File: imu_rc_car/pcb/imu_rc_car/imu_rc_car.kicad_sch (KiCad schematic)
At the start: 27 parts, among them J1 Encoder FS, J10 Prox Sensor RS, J11 Prox Sensor LS, J12 Prox Sensor BS, J2 Encoder BS, J7 Left Terminal, J8 Right Terminal, J9 Prox Sensor FS, Q5 IRLML6344TRPBF, Q6 DMP3160L-7, U1 ESP32-S3-DevKitC, U2 TB6612FNG, U3 AP2112K-3.3, U4 TB6612FNG

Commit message: commit #27
revision for hand unit complete (board is ready)
board for proximity sensors in series
minor revision in encoder board
progressing work in car board
added essential libraries support for 3D components
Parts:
- removed C7, C8: 1uF/16V, Capacitor_SMD:C_0805_2012Metric, symbol Device:C_Small
- removed J10: Prox Sensor RS, Connector_JST:JST_PH_S5B-PH-K_1x05_P2.00mm_Horizontal, symbol Connector:Conn_01x05_Socket
- removed J11: Prox Sensor LS, Connector_JST:JST_PH_S5B-PH-K_1x05_P2.00mm_Horizontal, symbol Connector:Conn_01x05_Socket
- removed J12: Prox Sensor BS, Connector_JST:JST_PH_S5B-PH-K_1x05_P2.00mm_Horizontal, symbol Connector:Conn_01x05_Socket
- removed J2: Encoder BS, Connector_JST:JST_PH_S4B-PH-K_1x04_P2.00mm_Horizontal, symbol Connector:Conn_01x04_Socket
- removed U3: AP2112K-3.3, Package_TO_SOT_SMD:SOT-23-5, symbol Regulator_Linear:AP2112K-3.3
- added C1: 10uF, Capacitor_SMD:CP_Elec_5x5.7, symbol Device:C_Polarized
- added J1: LiPo Battery, IMURCLibrary:AMASS_XT60IPW-M_1x03_P7.20mm_Horizontal, symbol Connector:Conn_01x02_Socket
- added J3: Encoder B, IMURCLibrary:JST_PH_S4B-PH-SM4-TB_1x04-1MP_P2.00mm_Horizontal, symbol Connector:Conn_01x04_Socket
- added J5: Prox Sensor LS, IMURCLibrary:JST_PH_S5B-PH-SM4-TB_1x05-1MP_P2.00mm_Horizontal, symbol Connector:Conn_01x05_Socket
- added J6: Prox Sensor RS, IMURCLibrary:JST_PH_S5B-PH-SM4-TB_1x05-1MP_P2.00mm_Horizontal, symbol Connector:Conn_01x05_Socket
- added J7: Prox Sensor BS, IMURCLibrary:JST_PH_S5B-PH-SM4-TB_1x05-1MP_P2.00mm_Horizontal, symbol Connector:Conn_01x05_Socket
- added JP1: SolderJumper_2_Open, Jumper:SolderJumper-2_P1.3mm_Open_RoundedPad1.0x1.5mm, symbol Jumper:SolderJumper_2_Open
- added SW1: SW_Nidec_CAS-120A1, Button_Switch_SMD:Nidec_Copal_CAS-120A, symbol Switch:SW_Nidec_CAS-120A1
- J2: renamed from J1; value Encoder FS -> Encoder F; footprint Connector_JST:JST_PH_S4B-PH-K_1x04_P2.00mm_Horizontal -> IMURCLibrary:JST_PH_S4B-PH-SM4-TB_1x04-1MP_P2.00mm_Horizontal
- J4: renamed from J9; footprint Connector_JST:JST_PH_S5B-PH-K_1x05_P2.00mm_Horizontal -> IMURCLibrary:JST_PH_S5B-PH-SM4-TB_1x05-1MP_P2.00mm_Horizontal
- J8: renamed from J7; footprint TerminalBlock:TerminalBlock_Xinya_XY308-2.54-4P_1x04_P2.54mm_Horizontal -> IMURCLibrary:TerminalBlock_Xinya_XY308-2.54-4P_1x04_P2.54mm_Horizontal
- J9: renamed from J8; footprint TerminalBlock:TerminalBlock_Xinya_XY308-2.54-4P_1x04_P2.54mm_Horizontal -> IMURCLibrary:TerminalBlock_Xinya_XY308-2.54-4P_1x04_P2.54mm_Horizontal
- R10: value 6k -> 51k
- R9: value 22k -> 33k
- U1: footprint PCM_Espressif:ESP32-S3-DevKitC -> IMURCLibrary:ESP32-S3-DevKitC
- renumbered Q6 to Q1, Q5 to Q2, U4 to U3
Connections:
- net 7.4V is gone; now on net +7V4: C11.1, C12.1, C15.1, C16.1, U2.13 (VM2), U2.14 (VM3), U2.24 (VM1), U3.13 (VM2), U3.14 (VM3), U3.24 (VM1)
- net SI is gone; now on net +7V4: J4.4 (Pin_4)
- net +3V3: now also J3.4 (Pin_4), J5.3 (Pin_3), J6.3 (Pin_3), J7.3 (Pin_3)
- net ENC3: now also J3.2 (Pin_2)
- net ENC4: now also J3.1 (Pin_1)
- net GND: now also C1.2, J1.1 (Pin_1), J3.3 (Pin_3), J5.2 (Pin_2), J6.2 (Pin_2), J7.2 (Pin_2)
- net PRX_BS: now also J7.1 (Pin_1)
- net PRX_LS: now also J5.1 (Pin_1)
- net PRX_RS: now also J6.1 (Pin_1)
- net SO: now also J7.5 (Pin_5)
- net at J4.5 (Pin_5): now also J5.4 (Pin_4), JP1.2 (B)
- net +BATT renamed +7V4
- net +7V4: now also C1.1, SW1.1 (C)
- net MOTOR1+ renamed MOTOR_FL+
- net MOTOR_FL+: now also J8.1 (Pin_1); no longer J8.2 (Pin_2)
- net MOTOR1- renamed MOTOR_FL-
- net MOTOR_FL-: now also J8.2 (Pin_2); no longer J8.1 (Pin_1)
- net MOTOR2+ renamed MOTOR_RL+
- net MOTOR2- renamed MOTOR_RL-
- net MOTOR3+ renamed MOTOR_RR+
- net MOTOR_RR+: now also J9.1 (Pin_1); no longer J9.2 (Pin_2)
- net MOTOR3- renamed MOTOR_RR-
- net MOTOR_RR-: now also J9.2 (Pin_2); no longer J9.1 (Pin_1)
- net MOTOR4+ renamed MOTOR_FR+
- net MOTOR4- renamed MOTOR_FR-
- new net: J5.5 (Pin_5), J6.4 (Pin_4)
- new net: J1.2 (Pin_2), SW1.2 (B)
- new net: J6.5 (Pin_5), J7.4 (Pin_4), JP1.1 (A)
- no-connect marks 0 -> 1
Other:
- note added: "Battery"
- note removed: "Voltage Regulator"
- moved on the sheet: C10, C11, C12, C13, C14, C15, C16, C9, J2, J4, J8, J9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

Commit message: commit #28
added 3d file for esp32s3
progression with car pcb
minor changes prox sensors test board
final revision hand unit
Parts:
- removed C10, C12, C14, C16: 10uF, Capacitor_SMD:C_1206_3216Metric_Pad1.33x1.80mm_HandSolder, symbol Device:C
- removed C11, C13, C15, C9: 0.1uF, Capacitor_SMD:C_1206_3216Metric_Pad1.33x1.80mm_HandSolder, symbol Device:C
- removed U2, U3: TB6612FNG, Package_SO:SSOP-24_5.3x8.2mm_P0.65mm, symbol Driver_Motor:TB6612FNG
- added C10, C12: 2.2uF, Capacitor_SMD:C_0805_2012Metric, symbol Device:C_Small
- added C11, C9: 10nF, Capacitor_SMD:C_0805_2012Metric, symbol Device:C_Small
- added C13, C15: 100nF, Capacitor_SMD:C_0805_2012Metric, symbol Device:C_Small
- added C14, C8: 10uF, Capacitor_SMD:C_0805_2012Metric, symbol Device:C_Small
- added Q1: IRLZ34N, Package_TO_SOT_SMD:TO-263-2_TabPin1, symbol Transistor_FET:IRLZ34N
- added R11: 22, Resistor_SMD:R_0805_2012Metric, symbol Device:R_US
- added R12: 100k, Resistor_SMD:R_0805_2012Metric, symbol Device:R_US
- added U3: AMS1117-3.3, Package_TO_SOT_SMD:SOT-223-3_TabPin2, symbol Regulator_Linear:AMS1117-3.3
- added U6, U7: DRV8833PWP, Package_SO:HTSSOP-16-1EP_4.4x5mm_P0.65mm_EP3.4x5mm_Mask2.46x2.31mm_ThermalVias, symbol Driver_Motor:DRV8833PWP
- J3: renamed from J1; footprint IMURCLibrary:AMASS_XT60IPW-M_1x03_P7.20mm_Horizontal -> TerminalBlock:TerminalBlock_MaiXu_MX126-5.0-02P_1x02_P5.00mm
- SW1: footprint Button_Switch_SMD:Nidec_Copal_CAS-120A -> Button_Switch_THT:SW_Slide_SPDT_Angled_CK_OS102011MA1Q
- U1: footprint IMURCLibrary:ESP32-S3-DevKitC -> PCM_Espressif:ESP32-S3-DevKitC
- renumbered J2 to J1, J5 to J10, J6 to J11, J7 to J12, J3 to J2, J8 to J7, J9 to J8, J4 to J9, Q2 to Q5, Q1 to Q6
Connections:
- net PWMA is gone; now on net BIN3: U1.6 (GPIO6/ADC1_CH5)
- net PWMB is gone; now on net BIN4: U1.7 (GPIO7/ADC1_CH6)
- net +3V3: now also C15.1, C8.1, U3.2 (VO)
- net +7V4: now also C10.1, C12.1, C13.1, C14.1, Q1.1 (G), R12.1, U3.3 (VI), U6.12 (VM), U6.14 (VINT), U7.12 (VM), U7.14 (VINT)
- net AIN1: now also U1.32 (GPIO35), U7.16 (AIN1); no longer U1.4 (GPIO4/ADC1_CH3)
- net AIN2: now also U1.30 (GPIO45), U7.15 (AIN2); no longer U1.5 (GPIO5/ADC1_CH4)
- net AIN3: now also U1.9 (GPIO16/ADC2_CH5/32K_N), U6.16 (AIN1); no longer U1.17 (GPIO11/ADC2_CH0)
- net AIN4: now also U1.8 (GPIO15/ADC2_CH4/32K_P), U6.15 (AIN2); no longer U1.18 (GPIO12/ADC2_CH1)
- net BATT_READ: now also U1.26 (GPIO20/USB_D+); no longer U1.32 (GPIO35)
- net BATT_READ_EN: now also U1.27 (GPIO21); no longer U1.33 (GPIO36)
- net BIN1: now also U1.28 (GPIO47), U7.9 (BIN1); no longer U1.11 (GPIO18/ADC2_CH7)
- net BIN2: now also U1.29 (GPIO48), U7.10 (BIN2); no longer U1.25 (GPIO19/USB_D-)
- net BIN3: now also U6.9 (BIN1); no longer U1.26 (GPIO20/USB_D+)
- net BIN4: now also U6.10 (BIN2); no longer U1.27 (GPIO21)
- net ENC1: now also U1.38 (GPIO41/MTDI)
- net ENC2: now also U1.39 (GPIO42/MTMS)
- net ENC3: now also U1.37 (GPIO40/MTDO)
- net ENC4: now also U1.36 (GPIO39/MTCK)
- net GND: now also C10.2, C11.2, C12.2, C13.2, C14.2, C15.2, C8.2, C9.2, R11.2, R12.2, U3.1 (GND), U6.13 (GND), U6.17 (GND), U6.3 (AISEN), U6.6 (BISEN), U7.13 (GND), U7.17 (GND), U7.3 (AISEN), U7.6 (BISEN)
- net MOTOR_FL+: now also U7.7 (BOUT1)
- net MOTOR_FL-: now also U7.5 (BOUT2)
- net MOTOR_FR+: now also J8.3 (Pin_3), U6.4 (AOUT2); no longer J8.4 (Pin_4)
- net MOTOR_FR-: now also J8.4 (Pin_4), U6.2 (AOUT1); no longer J8.3 (Pin_3)
- net MOTOR_RL+: now also J7.3 (Pin_3), U7.4 (AOUT2); no longer J7.4 (Pin_4)
- net MOTOR_RL-: now also J7.4 (Pin_4), U7.2 (AOUT1); no longer J7.3 (Pin_3)
- net MOTOR_RR+: now also U6.7 (BOUT1)
- net MOTOR_RR-: now also U6.5 (BOUT2)
- net PRX_BS: now also U1.5 (GPIO5/ADC1_CH4)
- net PRX_FS: now also U1.34 (GPIO37)
- net PRX_LS: now also U1.35 (GPIO38)
- net PRX_RS: now also U1.4 (GPIO4/ADC1_CH3)
- net SO: now also Q1.2 (D)
- net STBYA: now also U1.33 (GPIO36), U7.1 (~{SLEEP}); no longer U1.16 (GPIO10/ADC1_CH9)
- net STBYB: now also U6.1 (~{SLEEP})
- net PWMC: no longer names the net of U1.12 (GPIO8/ADC1_CH7)
- net PWMD: no longer names the net of U1.15 (GPIO9/ADC1_CH8)
- new net: C11.1, U7.11 (VCP)
- new net: C9.1, U6.11 (VCP)
- new net: Q1.3 (S), R11.1
- no-connect marks 1 -> 0
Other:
- note added: "Battery Conector"
- note added: "Esp32-S3-DevKit"
- note added: "PWM Prox Circuit"
- note added: "Voltage Regulator"
- note removed: "Battery"
- note removed: "Por os condensadores o mais perto dos drivers possivel"
- moved on the sheet: J1, J10, J11, J12, J2, J3, J7, J8, J9, JP1, Q5, Q6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

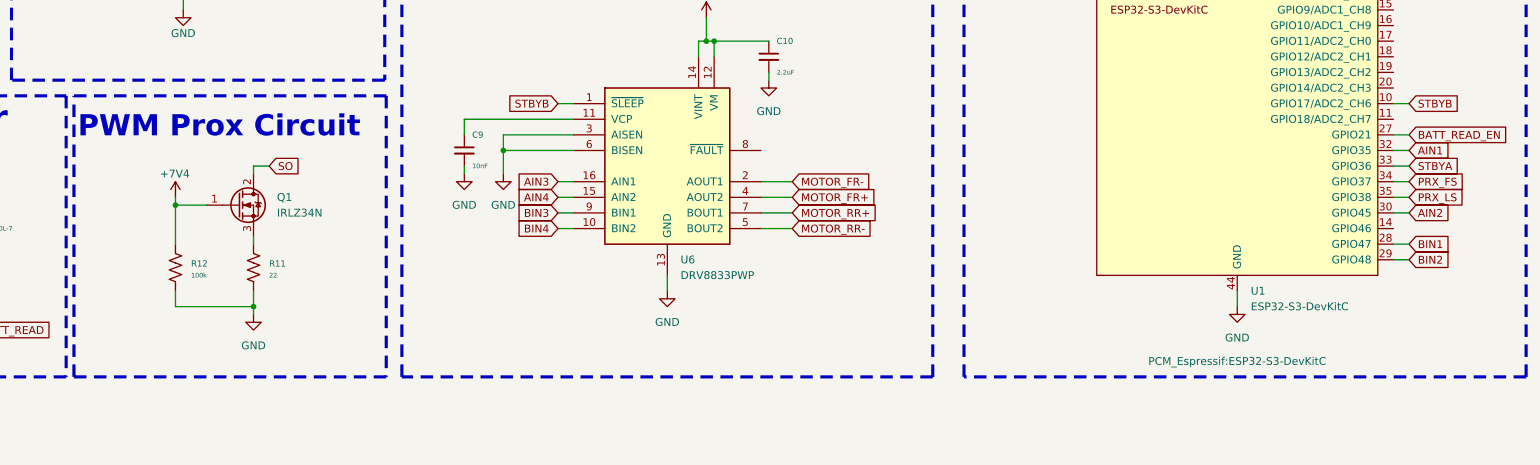
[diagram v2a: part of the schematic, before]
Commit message: commit #29
fixed board issue with PWM circuit driver
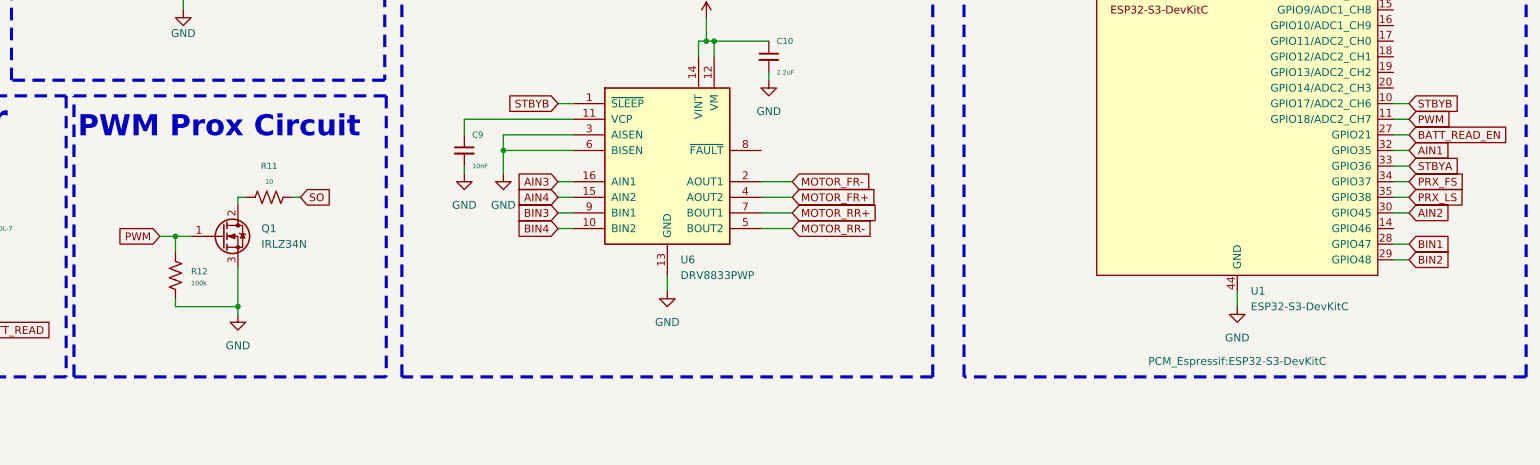
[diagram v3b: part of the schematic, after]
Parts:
- R11: value 22 -> 10
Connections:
- net +7V4: no longer Q1.1 (G), R12.1
- net GND: now also Q1.3 (S); no longer R11.2
- net SO: now also R11.2; no longer Q1.2 (D)
- net at R11.1: now also Q1.2 (D); no longer Q1.3 (S)
- net PWM: now reaches U1.11 (GPIO18/ADC2_CH7)
- net PWM: now also Q1.1 (G), R12.1
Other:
- moved on the sheet: Q1, R11, R12

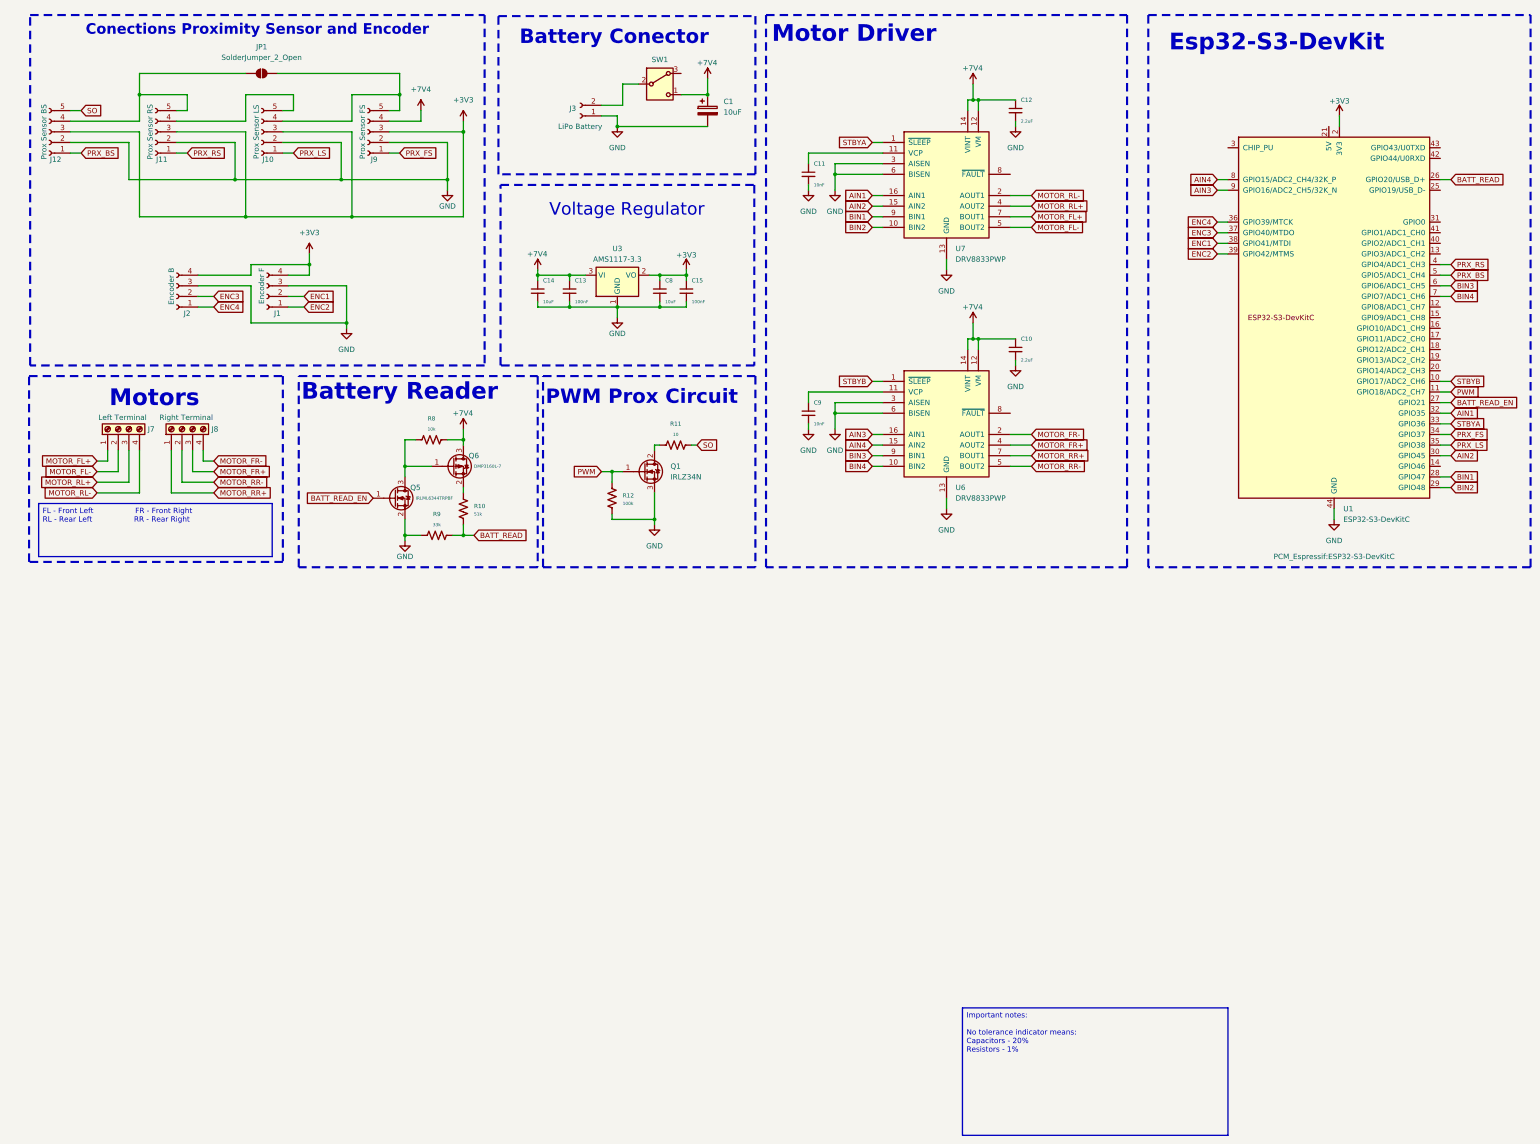
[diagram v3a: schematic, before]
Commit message: commit #30
changed 3d model offset in esp32s3
imported mouse-bites to kicad
final changes in imu-rc car before revision
critical change in pins 3 and 4 of optical sensor which were switched (encoder board)
removed test unit
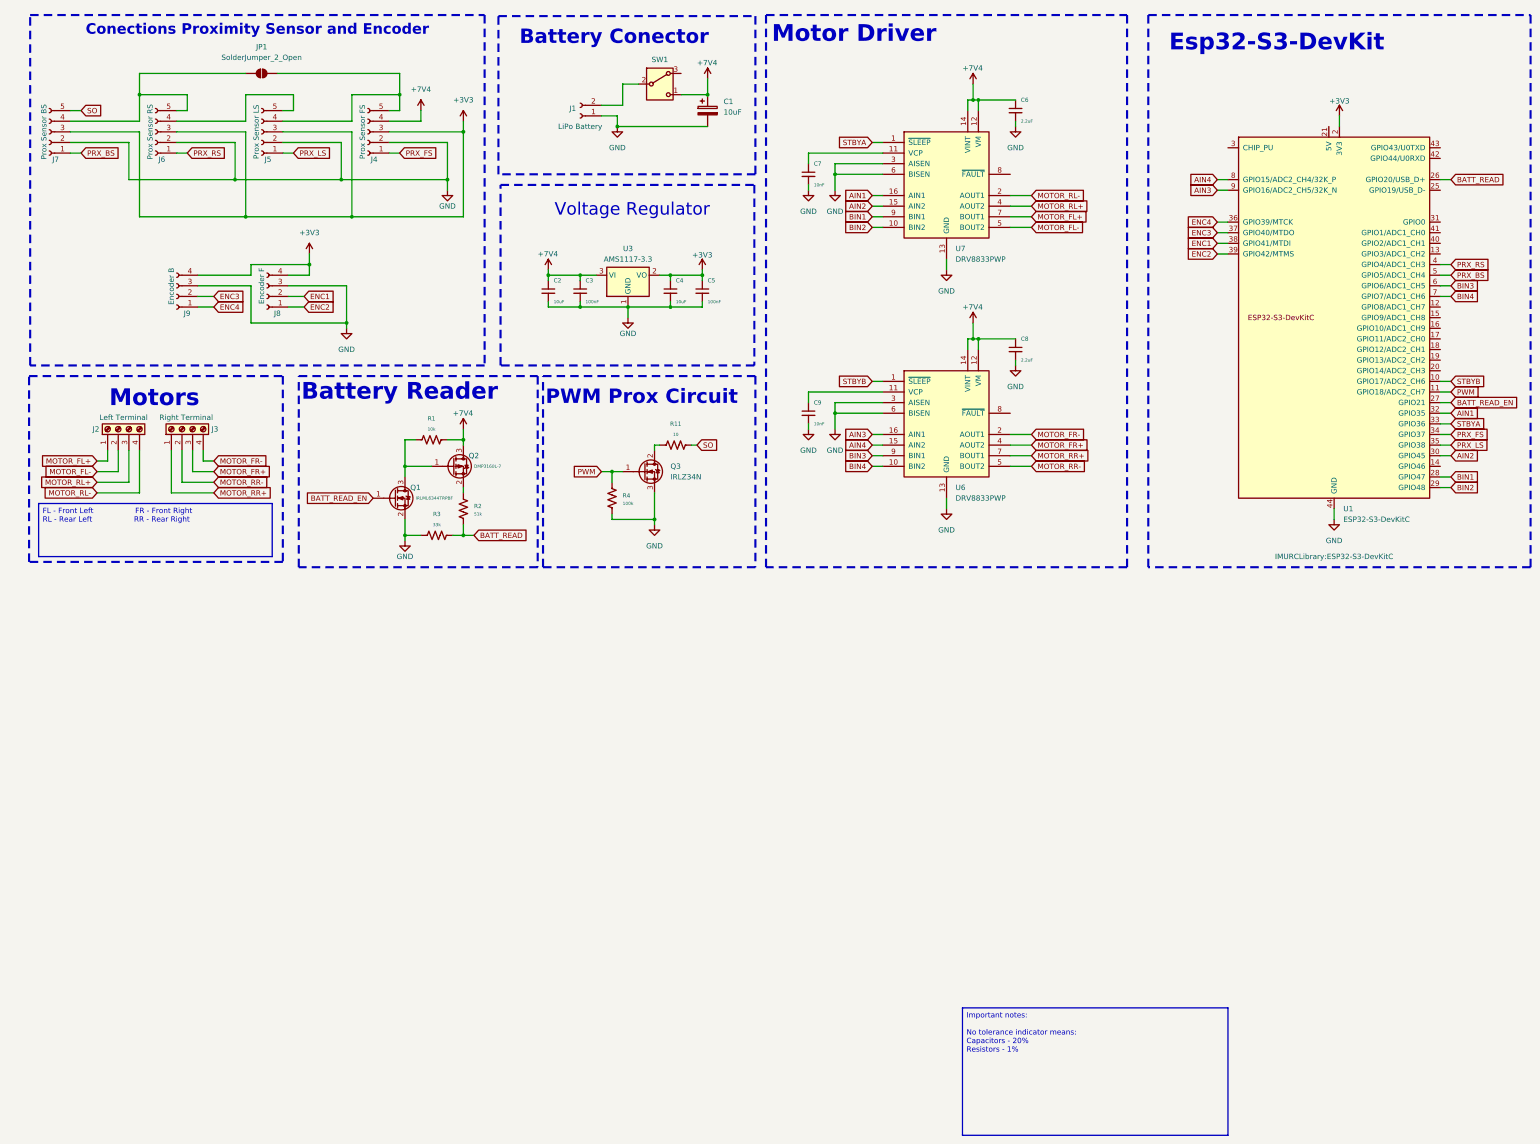
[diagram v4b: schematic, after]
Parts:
- removed J7: Left Terminal, IMURCLibrary:TerminalBlock_Xinya_XY308-2.54-4P_1x04_P2.54mm_Horizontal, symbol Connector:Screw_Terminal_01x04
- added J2: Left Terminal, IMURCLibrary:TerminalBlock_Xinya_XY308-2.54-4P_1x04_P2.54mm_Horizontal, symbol Connector:Screw_Terminal_01x04
- Q3: renamed from Q1; footprint Package_TO_SOT_SMD:TO-263-2_TabPin1 -> Package_TO_SOT_SMD:TO-263-3_TabPin2
- U1: footprint PCM_Espressif:ESP32-S3-DevKitC -> IMURCLibrary:ESP32-S3-DevKitC
- renumbered C14 to C2, C13 to C3, C8 to C4, C15 to C5, C12 to C6, C11 to C7, C10 to C8, J3 to J1, J8 to J3, J9 to J4, J10 to J5, J11 to J6, J12 to J7, J1 to J8, J2 to J9, Q5 to Q1, Q6 to Q2, R8 to R1, R10 to R2, R9 to R3, R12 to R4
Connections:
- net MOTOR_FL+: now also J2.1 (Pin_1)
- net MOTOR_FL-: now also J2.2 (Pin_2)
- net MOTOR_RL+: now also J2.3 (Pin_3)
- net MOTOR_RL-: now also J2.4 (Pin_4)
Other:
- moved on the sheet: C2, C3, C4, C5, U3
